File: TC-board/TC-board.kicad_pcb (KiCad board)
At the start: 2 copper layers, 63.5 x 63.5 mm, 13 parts, among them J1 DB15_Female, J2 PCIE-LP-01-01-F-DV-A-TR, J3 Conn_01x08_Male, J4 Conn_01x02_Male, J5 Conn_01x02_Male

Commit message: Updated pcie and fixed HX, MOSFET, TC board. Also added hierarchical sheet.
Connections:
- J2 pad B8: GND -> unconnected-(J2-PadB8)
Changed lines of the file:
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@@
   (net 50 "unconnected-(J2-PadB17)")
   (net 51 "unconnected-(J2-PadB18)")
+  (net 52 "unconnected-(J2-PadB8)")
   (footprint "Connector_PCBEdge:BUS_PCIexpress_x1" (layer "F.Cu")
     (at 145.034 106.68)
@@
       (net 48 "unconnected-(J2-PadB7)") (pinfunction "B7") (pintype "passive+no_connect"))
     (pad "B8" connect rect (at 7 0) (size 0.7 4.3) (layers "F.Cu" "F.Mask")
-      (net 1 "GND") (pinfunction "B8") (pintype "passive"))
+      (net 52 "unconnected-(J2-PadB8)") (pinfunction "B8") (pintype "passive+no_connect"))
     (pad "B9" connect rect (at 8 0) (size 0.7 4.3) (layers "F.Cu" "F.Mask")
       (net 30 "/CS1") (pinfunction "B9") (pintype "passive"))

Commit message: Revert "Revert "HX and TC Board mostly finished""
This reverts commit 2ae13608b6027366e1c59111a8dca91d16e06deb.
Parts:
- moved JP3 49.8 mm to (118.1, 96.7), turned to 180 degrees
- moved JP2 34.5 mm to (141.6, 94.2)
- moved JP1 29.7 mm to (141.1, 83.3)
- moved JP4 23.7 mm to (140.1, 88.6)
- moved J5 4.05 mm to (159.3, 84.6)
- moved J4 3.97 mm to (155.9, 92.6)
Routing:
- net GND: track 0.00 -> 210.0 mm, vias 0 -> 12
- net +3.3V: track 0.00 -> 162.3 mm, vias 0 -> 6
- net /SPI1_MISO: track 0.00 -> 121.4 mm, vias 0 -> 5
- net /SPI1_SCK: track 0.00 -> 110.5 mm, vias 0 -> 7
- net /TC4_T+: track 0.00 -> 70.7 mm
- net /TC4_T-: track 0.00 -> 63.3 mm, vias 0 -> 2
- net /TC2_T+: track 0.00 -> 53.4 mm, vias 0 -> 1
- net /TC2_T-: track 0.00 -> 47.7 mm
- net /CS3: track 0.00 -> 46.4 mm, vias 0 -> 2
- net /TC3_T+: track 0.00 -> 46.4 mm, vias 0 -> 4
- net /SPI0_MISO: track 0.00 -> 46.0 mm, vias 0 -> 2
- net /TC3_T-: track 0.00 -> 40.5 mm, vias 0 -> 4
- net /TC4_CS: track 0.00 -> 40.4 mm
- net /TC1_CS: track 0.00 -> 40.4 mm, vias 0 -> 2
- net /SPI0_SCK: track 0.00 -> 39.3 mm, vias 0 -> 2
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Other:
- board size 63.5 x 63.5 mm -> 63.5 x 63.6 mm

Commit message: Revert "HX and TC Board mostly finished"
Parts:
- moved JP3 49.8 mm to (159.8, 69.3), turned to 0 degrees
- moved JP2 34.5 mm to (159.5, 64.8)
- moved JP1 29.7 mm to (159.5, 59.9)
- moved JP4 23.7 mm to (158.5, 73.7)
- moved J5 4.05 mm to (159.1, 88.6)
- moved J4 3.97 mm to (159.1, 95.0)
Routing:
- net GND: track 210.0 -> 0.00 mm, vias 12 -> 0
- net +3.3V: track 162.3 -> 0.00 mm, vias 6 -> 0
- net /SPI1_MISO: track 121.4 -> 0.00 mm, vias 5 -> 0
- net /SPI1_SCK: track 110.5 -> 0.00 mm, vias 7 -> 0
- net /TC4_T+: track 70.7 -> 0.00 mm
- net /TC4_T-: track 63.3 -> 0.00 mm, vias 2 -> 0
- net /TC2_T+: track 53.4 -> 0.00 mm, vias 1 -> 0
- net /TC2_T-: track 47.7 -> 0.00 mm
- net /CS3: track 46.4 -> 0.00 mm, vias 2 -> 0
- net /TC3_T+: track 46.4 -> 0.00 mm, vias 4 -> 0
- net /SPI0_MISO: track 46.0 -> 0.00 mm, vias 2 -> 0
- net /TC3_T-: track 40.5 -> 0.00 mm, vias 4 -> 0
- net /TC4_CS: track 40.4 -> 0.00 mm
- net /TC1_CS: track 40.4 -> 0.00 mm, vias 2 -> 0
- net /SPI0_SCK: track 39.3 -> 0.00 mm, vias 2 -> 0
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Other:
- board size 63.5 x 63.6 mm -> 63.5 x 63.5 mm

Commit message: TC Board (mostly done) and HX Board Done (Mostly)
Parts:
- moved JP3 49.8 mm to (118.1, 96.7), turned to 180 degrees
- moved JP2 34.5 mm to (141.6, 94.2)
- moved JP1 29.7 mm to (141.1, 83.3)
- moved JP4 23.7 mm to (140.1, 88.6)
- moved J5 4.05 mm to (159.3, 84.6)
- moved J4 3.97 mm to (155.9, 92.6)
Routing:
- net GND: track 0.00 -> 210.0 mm, vias 0 -> 12
- net +3.3V: track 0.00 -> 162.3 mm, vias 0 -> 6
- net /SPI1_MISO: track 0.00 -> 121.4 mm, vias 0 -> 5
- net /SPI1_SCK: track 0.00 -> 110.5 mm, vias 0 -> 7
- net /TC4_T+: track 0.00 -> 70.7 mm
- net /TC4_T-: track 0.00 -> 63.3 mm, vias 0 -> 2
- net /TC2_T+: track 0.00 -> 53.4 mm, vias 0 -> 1
- net /TC2_T-: track 0.00 -> 47.7 mm
- net /TC3_T+: track 0.00 -> 46.4 mm, vias 0 -> 4
- net /SPI0_MISO: track 0.00 -> 46.0 mm, vias 0 -> 2
- net /CS3: track 0.00 -> 45.7 mm, vias 0 -> 2
- net /TC3_T-: track 0.00 -> 40.5 mm, vias 0 -> 4
- net /TC4_CS: track 0.00 -> 40.4 mm
- net /TC1_CS: track 0.00 -> 40.4 mm, vias 0 -> 2
- net /SPI0_SCK: track 0.00 -> 39.3 mm, vias 0 -> 2
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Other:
- board size 63.5 x 63.5 mm -> 63.5 x 63.6 mm

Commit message: Fixed TC
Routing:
- net /CS3: track 45.7 -> 46.4 mm
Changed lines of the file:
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@@
   (segment (start 120.3 63.4) (end 120.3 67.905416) (width 0.2) (layer "B.Cu") (net 14))
   (segment (start 117.6 93.2) (end 117.364 92.964) (width 0.254) (layer "F.Cu") (net 15))
-  (segment (start 120.1 96.7) (end 120.1 94.6) (width 0.254) (layer "F.Cu") (net 15))
   (segment (start 120.1 94.6) (end 119.8 94.3) (width 0.254) (layer "F.Cu") (net 15))
   (segment (start 117.364 92.964) (end 106.679 92.964) (width 0.254) (layer "F.Cu") (net 15))
+  (segment (start 120.1 96.7) (end 120.1 94.6) (width 0.254) (layer "F.Cu") (net 15))
   (via (at 117.6 93.2) (size 0.7112) (drill 0.3048) (layers "F.Cu" "B.Cu") (net 15))
   (via (at 119.8 94.3) (size 0.7112) (drill 0.3048) (layers "F.Cu" "B.Cu") (net 15))
@@
   (segment (start 148.857851 99.957851) (end 148.657851 99.957851) (width 0.254) (layer "B.Cu") (net 31))
   (segment (start 150.8 101.9) (end 148.857851 99.957851) (width 0.254) (layer "B.Cu") (net 31))
+  (segment (start 118.1 96.7) (end 118.1 98.3) (width 0.254) (layer "F.Cu") (net 32))
   (segment (start 154.4 102.2) (end 155.034 102.834) (width 0.254) (layer "F.Cu") (net 32))
+  (segment (start 118.1 98.3) (end 120.9 101.1) (width 0.254) (layer "F.Cu") (net 32))
   (segment (start 152.6636 102.2) (end 154.4 102.2) (width 0.254) (layer "F.Cu") (net 32))
-  (segment (start 118.1 97.018946) (end 122.181054 101.1) (width 0.254) (layer "F.Cu") (net 32))
-  (segment (start 122.181054 101.1) (end 145.8 101.1) (width 0.254) (layer "F.Cu") (net 32))
   (segment (start 152.09652 101.63292) (end 152.6636 102.2) (width 0.254) (layer "F.Cu") (net 32))
-  (segment (start 118.1 96.7) (end 118.1 97.018946) (width 0.254) (layer "F.Cu") (net 32))
   (segment (start 155.034 102.834) (end 155.034 106.68) (width 0.254) (layer "F.Cu") (net 32))
+  (segment (start 120.9 101.1) (end 145.8 101.1) (width 0.254) (layer "F.Cu") (net 32))
   (segment (start 151.93292 101.63292) (end 152.09652 101.63292) (width 0.254) (layer "F.Cu") (net 32))
   (via (at 145.8 101.1) (size 0.7112) (drill 0.3048) (layers "F.Cu" "B.Cu") (net 32))

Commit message: TC Board Done
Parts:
- moved JP3 57.4 mm to (158.5, 55.9), turned to 0 degrees
- moved JP4 25.8 mm to (160.1, 72.4), turned to 180 degrees
- moved JP1 25.0 mm to (158.9, 65.8)
- moved JP2 21.9 mm to (157.6, 79.3)
- moved J4 2.29 mm to (158.1, 91.9)
- moved J5 1.77 mm to (158.2, 85.9)
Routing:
- net /TC3_CS: track 16.2 -> 85.5 mm, vias 2 -> 3
- net GND: track 210.0 -> 150.2 mm, vias 12 -> 8
- net /TC1_CS: track 40.4 -> 67.4 mm, vias 2 -> 1
- net /TC4_CS: track 40.4 -> 62.2 mm, vias 0 -> 3
- net /CS1: track 29.4 -> 47.6 mm, vias 6 -> 4
- net /CS4: track 27.3 -> 41.0 mm, vias 5 -> 3
- net /CS3: track 46.4 -> 55.4 mm, vias 2 -> 4
- net /CS2: track 20.5 -> 28.9 mm, vias 2 -> 4
- net +3.3V: track 162.3 -> 155.3 mm, vias 6 -> 4
- net /SPI1_SCK: track 110.5 -> 105.7 mm, vias 7 -> 2
- net /TC2_T-: track 47.7 -> 51.8 mm
- net /TC2_CS: track 29.0 -> 31.9 mm, vias 4 -> 1
- net /SPI1_MISO: track 121.4 -> 124.2 mm, vias 5 -> 3
- net /TC4_T-: track 63.3 -> 65.3 mm
- net /TC2_T+: track 53.4 -> 55.1 mm, vias 1 -> 2
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- added copper zone on B.Cu, net GND
- added copper zone on F.Cu, net GND
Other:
- outline, holes or cut-outs redrawn
- board text added: "+3.3V"
- board text added: "GND"
- board text added: "SPI0_MISO"
- board text added: "SPI1_MISO"
- board text added: "SPI1_SCK"
- board text added: "SPIO_MISO"
- board text added: "SPIO_SCK"
- board text added: "TC1_CS"
- board text added: "TC1_T+"
- board text added: "TC1_T-"
- board text added: "TC2_CS"
- board text added: "TC2_T+"
- board text added: "TC2_T-"
- board text added: "TC3_CS"
- board text added: "TC3_T+"
- board text added: "TC3_T-"
- board text added: "TC4_CS"
- board text added: "TC4_T+"
- board text added: "TC4_T-"

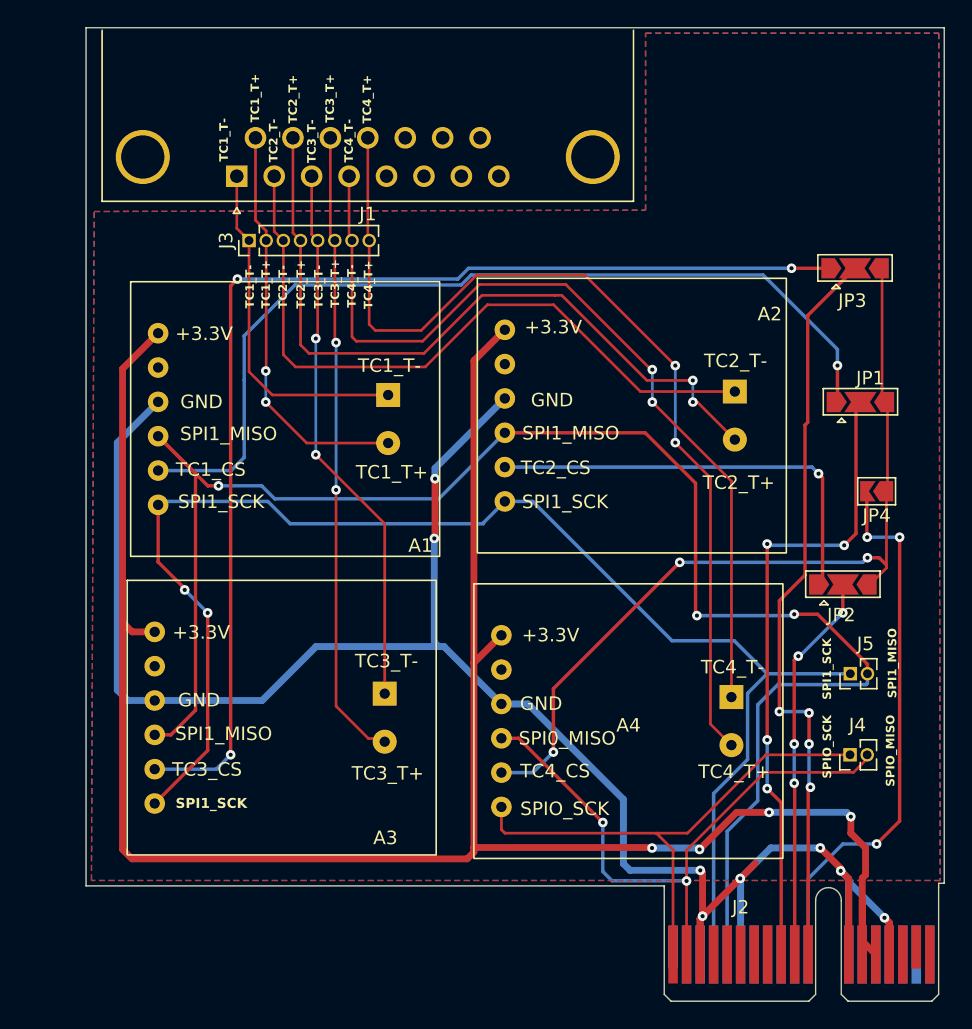
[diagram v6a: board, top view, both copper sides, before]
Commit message: Fixed labels for TC Board
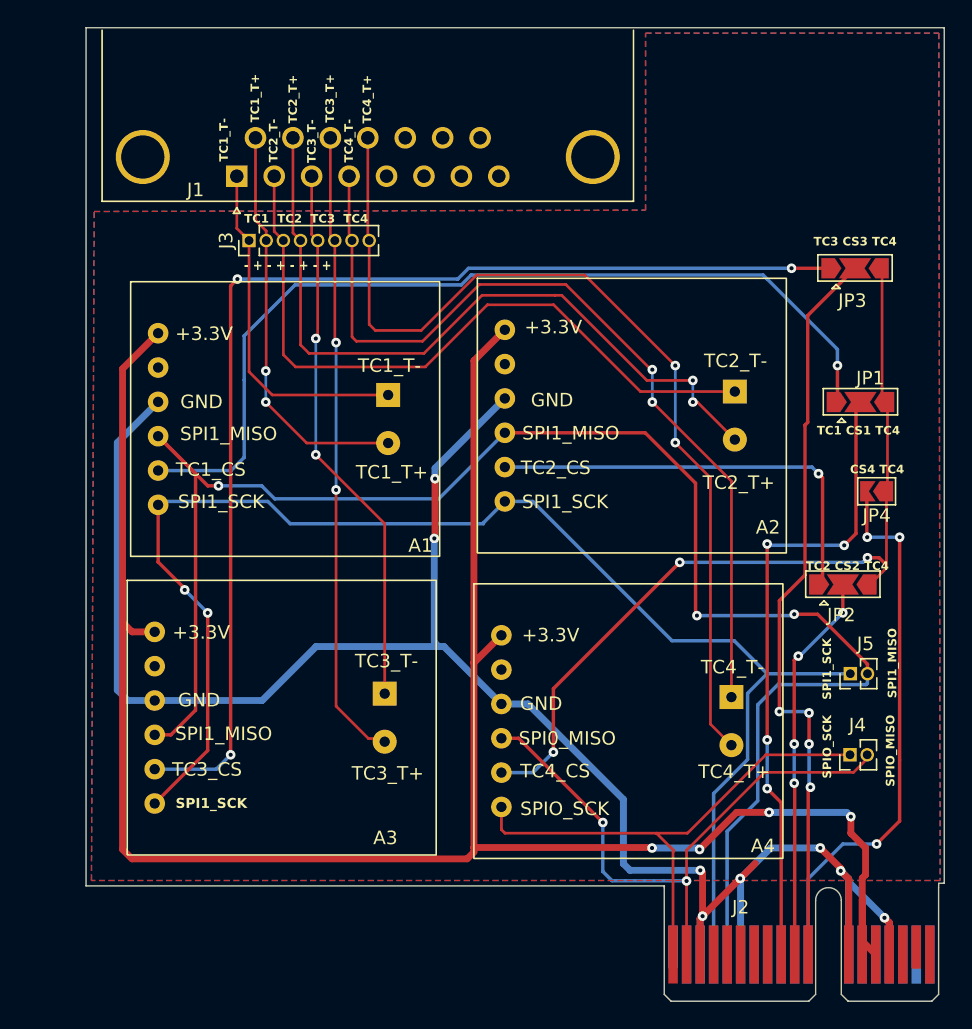
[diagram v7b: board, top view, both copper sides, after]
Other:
- board text added: "- + - + - + - +"
- board text added: "CS4 TC4"
- board text added: "TC1 CS1 TC4"
- board text added: "TC1 TC2 TC3 TC4"
- board text added: "TC2 CS2 TC4"
- board text added: "TC3 CS3 TC4"
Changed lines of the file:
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@@
     (property "Sheetname" "")
     (attr through_hole)
-    (fp_text reference "J1" (at -9.695 -2.8) (layer "F.SilkS")
+    (fp_text reference "J1" (at 3.053 -1.013669 180) (layer "F.SilkS")
         (effects (font (size 1 1) (thickness 0.15)))
     )
@@
     (property "Sheetname" "")
     (attr through_hole)
-    (fp_text reference "A2" (at -7.512 -10.204 unlocked) (layer "F.SilkS")
+    (fp_text reference "A2" (at 8.268 -10.074 unlocked) (layer "F.SilkS")
         (effects (font (size 1 1) (thickness 0.15)))
     )
@@
     (property "Sheetname" "")
     (attr through_hole)
-    (fp_text reference "A4" (at 0.312 -0.008 unlocked) (layer "F.SilkS")
+    (fp_text reference "A4" (at 9.232 -9.958 unlocked) (layer "F.SilkS")
         (effects (font (size 1 1) (thickness 0.15)))
     )
@@
     (effects (font (size 0.635 0.635) (thickness 0.127) bold) (justify left bottom))
   )
+  (gr_text "TC2 CS2 TC4" (at 154.85 78.3) (layer "F.SilkS")
+    (effects (font (size 0.635 0.635) (thickness 0.127) bold) (justify left bottom))
+  )
   (gr_text "TC3_T-" (at 121.49 85.55) (layer "F.SilkS")
     (effects (font (size 1 1) (thickness 0.15)) (justify left bottom))
@@
     (effects (font (size 1 1) (thickness 0.15)) (justify left bottom))
   )
-  (gr_text "TC2_T-" (at 116.54 58.89 90) (layer "F.SilkS")
-    (effects (font (size 0.635 0.635) (thickness 0.127) bold) (justify left bottom))
-  )
   (gr_text "+3.3V" (at 134.04 60.84) (layer "F.SilkS")
     (effects (font (size 1 1) (thickness 0.15)) (justify left bottom))
@@
     (effects (font (size 1 1) (thickness 0.15)) (justify left bottom))
   )
-  (gr_text "TC3_T+" (at 120.4 58.83 90) (layer "F.SilkS")
-    (effects (font (size 0.635 0.635) (thickness 0.127) bold) (justify left bottom))
-  )
   (gr_text "GND" (at 134.51 66.24) (layer "F.SilkS")
     (effects (font (size 1 1) (thickness 0.15)) (justify left bottom))
@@
     (effects (font (size 0.635 0.635) (thickness 0.127) bold) (justify left bottom))
   )
-  (gr_text "TC1_T+" (at 115.28 58.88 90) (layer "F.SilkS")
-    (effects (font (size 0.635 0.635) (thickness 0.127) bold) (justify left bottom))
+  (gr_text "- + - + - + - +" (at 113.275 56.125) (layer "F.SilkS")
+    (effects (font (size 0.762 0.635) (thickness 0.127) bold) (justify left bottom))
   )
   (gr_text "TC1_T+" (at 114.48 45.11 90) (layer "F.SilkS")
@@
     (effects (font (size 1 1) (thickness 0.15)) (justify left bottom))
   )
-  (gr_text "TC2_T+" (at 117.87 58.89 90) (layer "F.SilkS")
-    (effects (font (size 0.635 0.635) (thickness 0.127) bold) (justify left bottom))
-  )
   (gr_text "TC3_CS" (at 107.96 93.57) (layer "F.SilkS")
     (effects (font (size 1 1) (thickness 0.15)) (justify left bottom))
@@
     (effects (font (size 1 1) (thickness 0.15)) (justify left bottom))
   )
+  (gr_text "TC3 CS3 TC4" (at 155.43 54.29) (layer "F.SilkS")
+    (effects (font (size 0.635 0.635) (thickness 0.127) bold) (justify left bottom))
+  )
+  (gr_text "TC1  TC2  TC3  TC4" (at 113.3 52.6) (layer "F.SilkS")
+    (effects (font (size 0.635 0.635) (thickness 0.127) bold) (justify left bottom))
+  )
+  (gr_text "CS4 TC4" (at 158.125 71.15) (layer "F.SilkS")
+    (effects (font (size 0.635 0.635) (thickness 0.127) bold) (justify left bottom))
+  )
   (gr_text "SPI1_SCK" (at 108.4 73.76) (layer "F.SilkS")
     (effects (font (size 1 1) (thickness 0.15)) (justify left bottom))
@@
     (effects (font (size 0.635 0.635) (thickness 0.127) bold) (justify left bottom))
   )
-  (gr_text "TC4_T-" (at 121.63 58.82 90) (layer "F.SilkS")
-    (effects (font (size 0.635 0.635) (thickness 0.127) bold) (justify left bottom))
-  )
-  (gr_text "TC1_T-\n" (at 114.09 58.87 90) (layer "F.SilkS")
-    (effects (font (size 0.635 0.635) (thickness 0.127) bold) (justify left bottom))
-  )
   (gr_text "SPIO_SCK\n" (at 156.81 93.66 90) (layer "F.SilkS")
-    (effects (font (size 0.635 0.635) (thickness 0.127) bold) (justify left bottom))
-  )
-  (gr_text "TC4_T+" (at 122.86 58.92 90) (layer "F.SilkS")
-    (effects (font (size 0.635 0.635) (thickness 0.127) bold) (justify left bottom))
-  )
-  (gr_text "TC3_T-" (at 119.18 58.88 90) (layer "F.SilkS")
     (effects (font (size 0.635 0.635) (thickness 0.127) bold) (justify left bottom))
   )
@@
     (effects (font (size 0.7366 0.7366) (thickness 0.14986) bold) (justify left bottom))
   )
+  (gr_text "TC1 CS1 TC4" (at 155.675 68.275) (layer "F.SilkS")
+    (effects (font (size 0.635 0.635) (thickness 0.127) bold) (justify left bottom))
+  )
   (segment (start 147.034 106.68) (end 147.034 104.022) (width 0.508) (layer "F.Cu") (net 1))
